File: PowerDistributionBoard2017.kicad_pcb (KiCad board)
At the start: 2 copper layers, 119.6 x 57.4 mm, 28 parts, among them J1 Main Computer (Jetson), J10 Drive 1, J11 Drive 2, J12 Drive 3, J13 Drive 4, J14 Digger 1, J15 Digger 2, J16 Bucket 1, J17 Bucket 2, J18 MAux 1, J19 Conn_02x02_Counter_Clockwise, J2 IMU, J3 Localization, J4 Second Computer, J5 Aux 1, J6 Aux 2, J7 Aux 3, J8 Main Button, J9 JM Button, K1 FINDER-36.11-4301, K2 FINDER-36.11-4301

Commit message: Continued layout
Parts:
- turned D2 to 180 degrees
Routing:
- net Net-(D3-Pad1): track 0.00 -> 41.5 mm
- net /EBM: track 0.00 -> 35.3 mm, vias 0 -> 1
- net Net-(D4-Pad1): track 0.00 -> 31.5 mm
- added copper zone on F.Cu, net /Batman
- added copper zone on F.Cu, net /EBM
- added copper zone on F.Cu, net /JM
- added copper zone on B.Cu, net GND
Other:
- rule trace_min: 0.2 -> 0.1524
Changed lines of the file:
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@@
   (general
     (links 55)
-    (no_connects 55)
+    (no_connects 51)
     (area 123.124999 64.724999 242.875001 122.275001)
     (thickness 1.6)
     (drawings 4)
-    (tracks 0)
+    (tracks 16)
     (zones 0)
     (modules 28)
@@
     (zone_clearance 0.508)
     (zone_45_only no)
-    (trace_min 0.2)
+    (trace_min 0.1524)
     (segment_width 0.2)
     (edge_width 0.15)
@@
     (pad_to_mask_clearance 0.2)
     (aux_axis_origin 0 0)
-    (visible_elements FFFFFF7F)
+    (visible_elements 7FFFFFFF)
     (pcbplotparams
       (layerselection 0x00030_80000001)
@@
   )
   (module LEDs:LED_1206_HandSoldering (layer F.Cu)
-    (at 213.4 118.95)
+    (at 213.4 118.95 180)
     (descr "LED SMD 1206, hand soldering")
     (tags "LED 1206")
     (attr smd)
-    (fp_text reference D2 (at 0 -1.85) (layer F.SilkS)
-      (effects (font (size 1 1) (thickness 0.15)))
-    )
-    (fp_text value "Second PWR LED" (at 0 1.9) (layer F.Fab)
+    (fp_text reference D2 (at 0 -1.85 180) (layer F.SilkS)
+      (effects (font (size 1 1) (thickness 0.15)))
+    )
+    (fp_text value "Second PWR LED" (at 0 1.9 180) (layer F.Fab)
       (effects (font (size 1 1) (thickness 0.15)))
     )
@@
     (fp_line (start 3.25 1.1) (end 3.25 -1.11) (layer F.CrtYd) (width 0.05))
     (fp_line (start 3.25 1.1) (end -3.25 1.1) (layer F.CrtYd) (width 0.05))
-    (pad 1 smd rect (at -2 0) (size 2 1.7) (layers F.Cu F.Paste F.Mask)
-      (net 1 GND))
-    (pad 2 smd rect (at 2 0) (size 2 1.7) (layers F.Cu F.Paste F.Mask)
+    (pad 1 smd rect (at -2 0 180) (size 2 1.7) (layers F.Cu F.Paste F.Mask)
+      (net 1 GND))
+    (pad 2 smd rect (at 2 0 180) (size 2 1.7) (layers F.Cu F.Paste F.Mask)
       (net 3 "Net-(D2-Pad2)"))
     (model ${KISYS3DMOD}/LEDs.3dshapes/LED_1206.wrl
@@
       (effects (font (size 1 1) (thickness 0.15)))
     )
-    (fp_text value "JM Button" (at 0 10.5) (layer F.Fab)
+    (fp_text value "JM Button" (at 0.1 8.95) (layer F.Fab)
       (effects (font (size 1 1) (thickness 0.15)))
     )
@@
   (gr_line (start 123.2 122.2) (end 242.8 122.2) (angle 90) (layer Edge.Cuts) (width 0.15))
   (gr_line (start 123.2 64.8) (end 123.2 122.2) (angle 90) (layer Edge.Cuts) (width 0.15))
+  (segment (start 167.65 118.95) (end 167.65 104.3) (width 0.25) (layer F.Cu) (net 4))
+  (segment (start 167.65 104.3) (end 169.75 102.2) (width 0.25) (layer F.Cu) (net 4))
+  (segment (start 162.2 81.45) (end 162.25 81.45) (width 0.25) (layer F.Cu) (net 4))
+  (segment (start 162.25 81.45) (end 166.4 85.6) (width 0.25) (layer F.Cu) (net 4))
+  (segment (start 166.4 85.6) (end 166.4 98.85) (width 0.25) (layer F.Cu) (net 4))
+  (segment (start 166.4 98.85) (end 169.75 102.2) (width 0.25) (layer F.Cu) (net 4))
+  (segment (start 193.45 118.95) (end 193.45 110.75) (width 0.25) (layer F.Cu) (net 5))
+  (segment (start 202 102.2) (end 213.2 102.2) (width 0.25) (layer F.Cu) (net 5))
+  (segment (start 193.45 110.75) (end 202 102.2) (width 0.25) (layer F.Cu) (net 5))
+  (segment (start 184.9 86.95) (end 184.9 91.9) (width 0.25) (layer F.Cu) (net 8))
+  (segment (start 200.9 111.7) (end 204.8 111.7) (width 0.25) (layer B.Cu) (net 8))
+  (segment (start 193 103.8) (end 200.9 111.7) (width 0.25) (layer B.Cu) (net 8))
+  (segment (start 193 100) (end 193 103.8) (width 0.25) (layer B.Cu) (net 8))
+  (segment (start 190.6 97.6) (end 193 100) (width 0.25) (layer B.Cu) (net 8))
+  (via (at 190.6 97.6) (size 0.6) (drill 0.4) (layers F.Cu B.Cu) (net 8))
+  (segment (start 184.9 91.9) (end 190.6 97.6) (width 0.25) (layer F.Cu) (net 8))
+  (zone (net 1) (net_name GND) (layer B.Cu) (hatch edge 0.508)
+    (connect_pads (clearance 0.508))
+    (min_thickness 0.254)
+    (fill (arc_segments 16) (thermal_gap 0.508) (thermal_bridge_width 0.508))
+    (polygon
+      (pts
+        (xy 242.8 65) (xy 242.8 122.2) (xy 123.2 122.2) (xy 123.2 64.8)
+      )
+    )
+  )
+  (zone (net 9) (net_name /JM) (layer F.Cu) (hatch edge 0.508)
+    (connect_pads (clearance 0.508))
+    (min_thickness 0.254)
+    (fill (arc_segments 16) (thermal_gap 0.508) (thermal_bridge_width 0.508))
+    (polygon
+      (pts
+        (xy 189.8 65) (xy 242.6 64.8) (xy 242.6 122.2) (xy 218.4 122) (xy 218.4 89.4)
+        (xy 189.8 89.2) (xy 189.6 65)
+      )
+    )
+  )
+  (zone (net 8) (net_name /EBM) (layer F.Cu) (hatch edge 0.508)
+    (connect_pads (clearance 0.508))
+    (min_thickness 0.254)
+    (fill (arc_segments 16) (thermal_gap 0.508) (thermal_bridge_width 0.508))
+    (polygon
+      (pts
+        (xy 157.4 89.6) (xy 164 89.6) (xy 164 96.6) (xy 148.2 96.6) (xy 148.2 122.2)
+        (xy 123.2 122.2) (xy 123.2 64.8) (xy 157.4 64.8)
+      )
+    )
+  )
+  (zone (net 7) (net_name /Batman) (layer F.Cu) (hatch edge 0.508)
+    (connect_pads (clearance 0.508))
+    (min_thickness 0.254)
+    (fill (arc_segments 16) (thermal_gap 0.508) (thermal_bridge_width 0.508))
+    (polygon
+      (pts
+        (xy 188.6 66) (xy 189 90) (xy 217.2 90) (xy 217.2 115.6) (xy 148.8 115.6)
+        (xy 148.8 97.4) (xy 164.6 97.4) (xy 164.6 89.2) (xy 158.4 89) (xy 158.4 87.6)
+        (xy 158.4 65.8)
+      )
+    )
+  )
 )

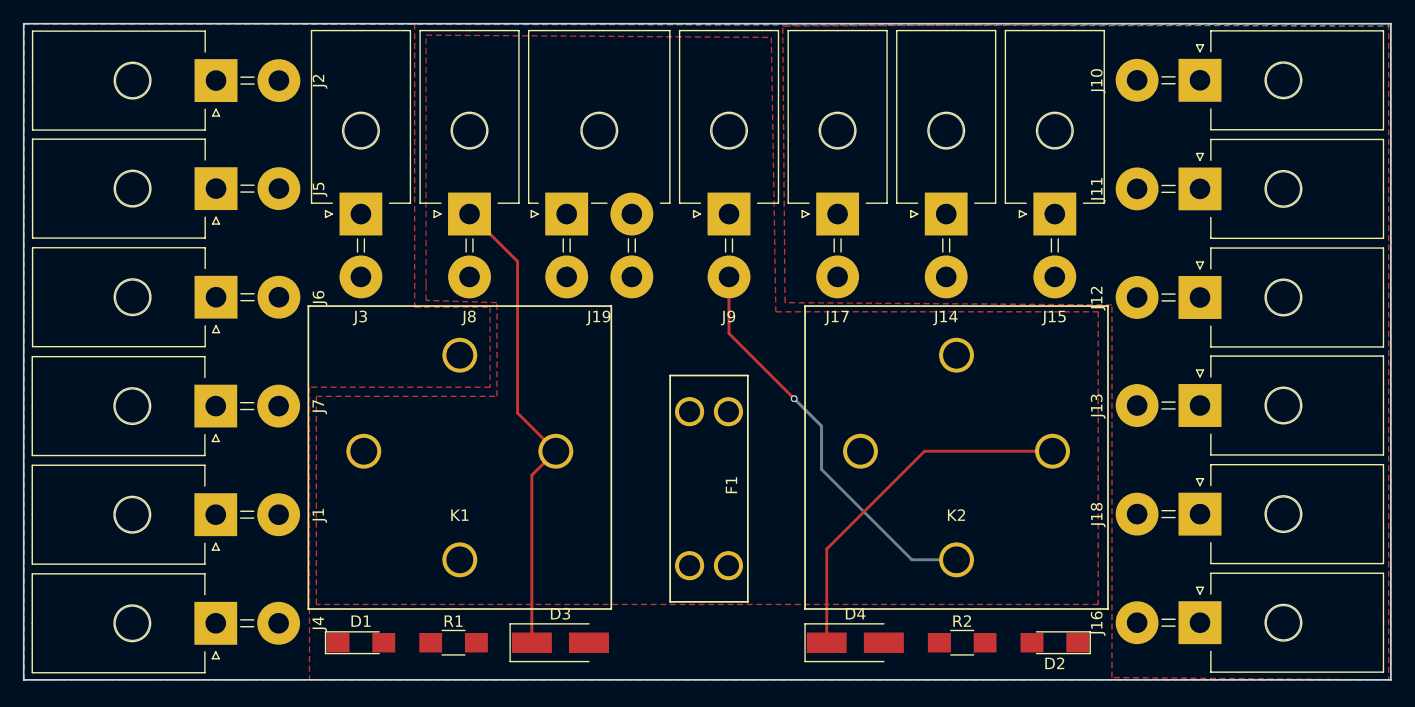
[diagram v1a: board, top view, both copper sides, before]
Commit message: Routing Finished, Needs silkscreen and trace size verification
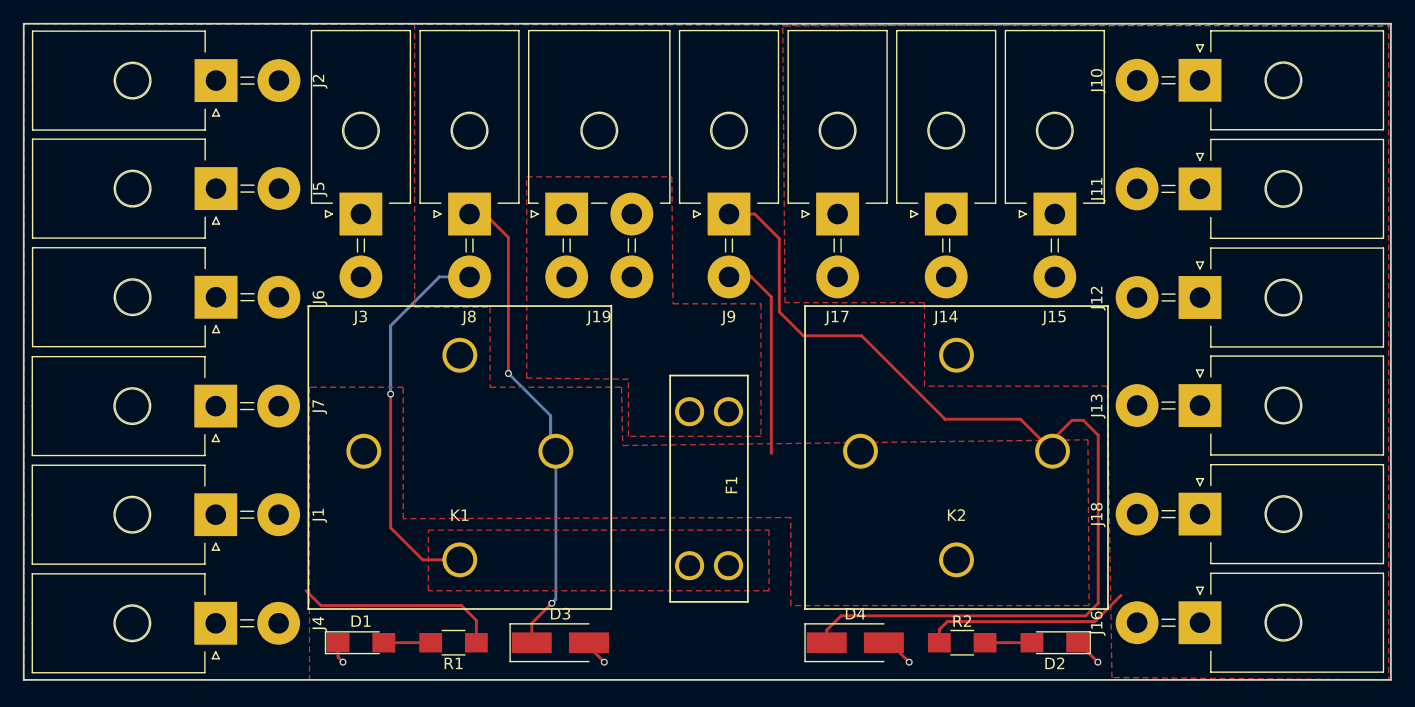
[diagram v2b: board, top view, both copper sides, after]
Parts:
- turned R1 to 180 degrees
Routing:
- net Net-(D4-Pad1): track 31.5 -> 87.4 mm
- net Net-(F1-Pad1): track 0.00 -> 34.1 mm, vias 0 -> 1
- net /JM: track 0.00 -> 18.3 mm
- net GND: track 0.00 -> 9.52 mm, vias 0 -> 4
- net Net-(D1-Pad2): track 0.00 -> 4.10 mm
- net Net-(D2-Pad2): track 0.00 -> 4.10 mm
- net Net-(D3-Pad1): track 41.5 -> 43.7 mm, vias 0 -> 2
- net /EBM: track 35.3 -> 36.1 mm, vias 1 -> 0
- added copper zone on F.Cu, net Net-(F1-Pad1)

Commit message: Generated Gerbers and added silkscreen
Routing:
- net Net-(D3-Pad1): track 43.7 -> 44.4 mm
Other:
- board text added: "+12V on square pins GND on circle pins"
- board text added: "Batt"
- board text added: "Designed by USR in Utah Made in the USA Tina Hayward & Cole Mortensen"
- board text added: "JM"
- board text added: "Main"
- board text added: "Power Distribution Board (2017-18)"
